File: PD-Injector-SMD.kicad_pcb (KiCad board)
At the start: 2 copper layers, 18.4 x 28 mm, 25 parts, among them P1 USB_C_Plug_USB2.0

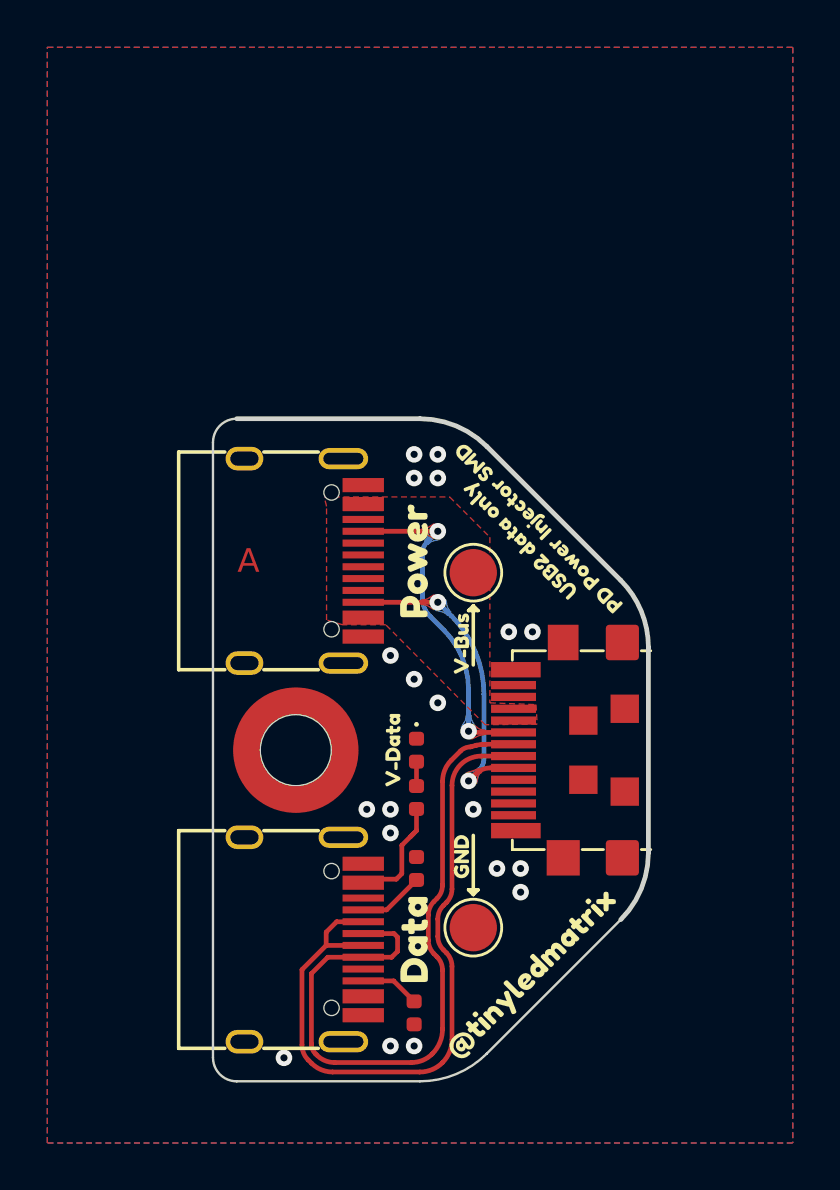
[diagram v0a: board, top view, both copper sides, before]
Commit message: Swapped output to receptacle
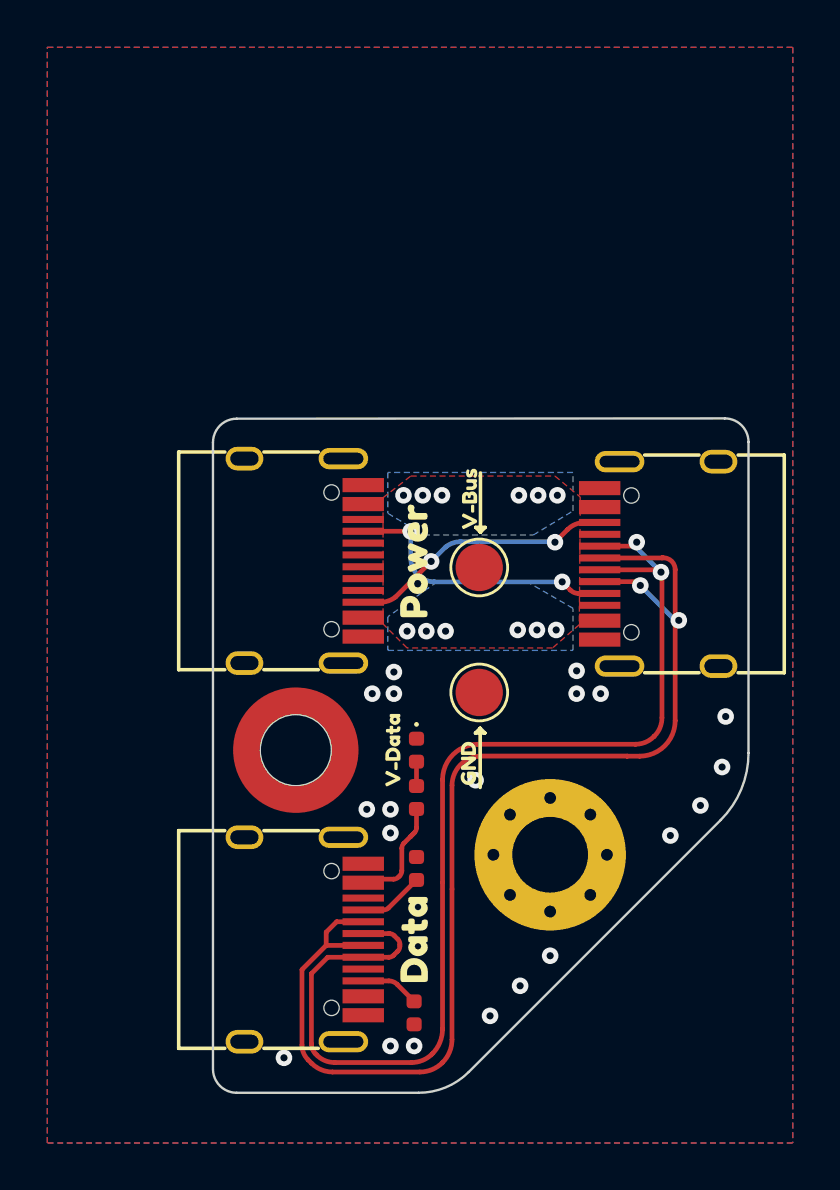
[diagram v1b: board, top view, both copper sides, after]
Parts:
- removed P1: USB_C_Plug_USB2.0, Connector_USB_Extra:USB_C_Plug_UTC009-C12
- removed kibuzzard-63336840: G***, kibuzzard-63336840
- removed kibuzzard-6333684F: G***, kibuzzard-6333684F
- removed kibuzzard-63337211: G***, kibuzzard-63337211
- removed kibuzzard-63337259: G***, kibuzzard-63337259
- removed kibuzzard-6333729D: G***, kibuzzard-6333729D
- removed kibuzzard-633372BC: G***, kibuzzard-633372BC
- removed kibuzzard-633372D7: G***, kibuzzard-633372D7
- removed kibuzzard-6334B4B7: G***, kibuzzard-6334B4B7
- removed kibuzzard-6334B4C9: G***, kibuzzard-6334B4C9
- removed kibuzzard-6334B502: G***, kibuzzard-6334B502
- added MK1: M3, Mounting_Holes:MountingHole_3.2mm_M3_Pad_Via, F.Cu at (170.7, 90.4)
- added USB-C3: USB_C_Receptacle_USB2.0, PD-Injector_SMD:USB_C_Receptacle_GT-USB-7010, F.Cu at (176.0, 78.1)
- moved TP2 9.94 mm to (167.8, 83.6)
- moved kibuzzard-6334B838 6.13 mm to (167.3, 75.4)
- moved kibuzzard-6334B904 3.95 mm to (167.3, 86.6)
- moved TP1 0.33 mm to (167.8, 78.3)
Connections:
- USB-C2 pad A9: unconnected-(USB-C2-PadA9) -> Net-(USB-C2-VBUS-PadA9)
- USB-C2 pad B4: unconnected-(USB-C2-PadA9) -> Net-(USB-C2-VBUS-PadA9)
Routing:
- net /D-: track 30.5 -> 51.7 mm, vias 0 -> 2
- net /D+: track 30.5 -> 49.3 mm, vias 0 -> 2
- net /CC1P: track 14.3 -> 11.8 mm
- net /CC2P: track 13.6 -> 11.3 mm
- net VBUS: vias 0 -> 12
- net GND: vias 19 -> 20
- added copper zone on B.Cu, net VBUS
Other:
- board size 18.4 x 28 mm -> 22.6 x 28.5 mm
- board text added: "DATA"
- board text added: "DATA+POWER"
- board text added: "POWER"
- board text removed: "A"

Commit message: Update readme, minor mucking about
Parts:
- USB-C1, USB-C2: footprint Connector_USB_Extra:USB_C_Receptacle_GT-USB-7010 -> PD-Injector_SMD:USB_C_Receptacle_GT-USB-7010
